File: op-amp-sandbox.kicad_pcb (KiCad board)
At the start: 2 copper layers, 14 parts, among them J1 Conn_01x06, J2 Conn_01x04, U2 TLV2372

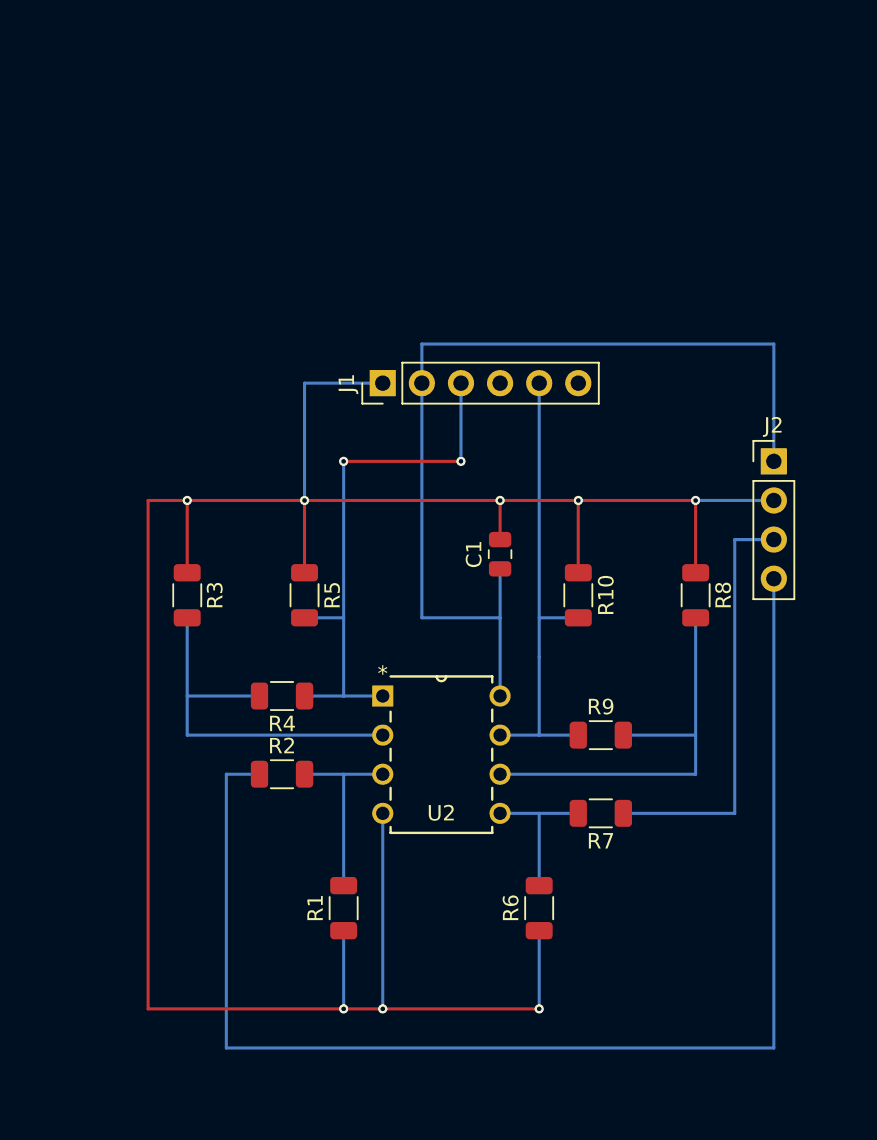
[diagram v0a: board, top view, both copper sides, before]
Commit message: Added additional pin headers to the board.
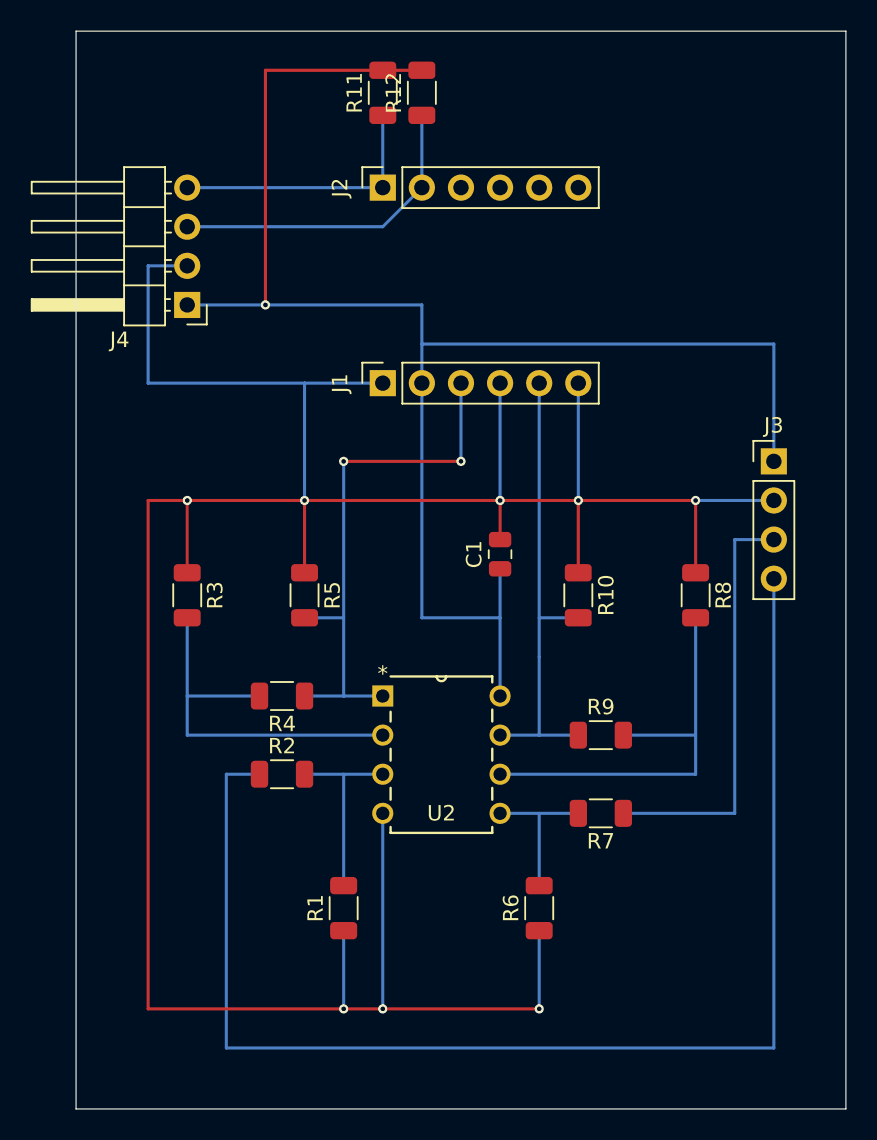
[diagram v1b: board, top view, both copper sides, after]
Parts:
- added J3: Conn_01x04, Connector_PinHeader_2.54mm:PinHeader_1x04_P2.54mm_Vertical, F.Cu at (160.0, 86.4)
- added J4: Conn_01x04, Connector_PinHeader_2.54mm:PinHeader_1x04_P2.54mm_Horizontal, F.Cu at (121.9, 76.2)
- added R11: 4.7k, Resistor_SMD:R_1206_3216Metric, F.Cu at (134.6, 62.4)
- added R12: 4.7k, Resistor_SMD:R_1206_3216Metric, F.Cu at (137.2, 62.4)
- J1: footprint Connector_PinHeader_2.54mm:PinHeader_1x06_P2.54mm_Vertical -> Connector_PinSocket_2.54mm:PinSocket_1x06_P2.54mm_Vertical
- J2: value Conn_01x04 -> Conn_01x06; footprint Connector_PinHeader_2.54mm:PinHeader_1x04_P2.54mm_Vertical -> Connector_PinSocket_2.54mm:PinSocket_1x06_P2.54mm_Vertical
- moved J2 31.0 mm to (134.6, 68.6), turned to 90 degrees
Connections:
- J1 pad 4: unconnected-(J1-Pin_4-Pad4) -> GND
- J1 pad 6: unconnected-(J1-Pin_6-Pad6) -> GND
- J2 pad 1: VCC -> SCL
- J2 pad 2: GND -> SDA
- J2 pad 3: Net-(J2-Pin_3) -> unconnected-(J2-Pin_3-Pad3)
- J2 pad 4: in -> unconnected-(J2-Pin_4-Pad4)
- R7 pad 1: Net-(J2-Pin_3) -> Net-(J3-Pin_3)
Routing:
- net VCC: track 61.6 -> 104.8 mm, vias 0 -> 1
- net GND: track 155.9 -> 191.5 mm
- net Net-(J3-Pin_3): track 0.00 -> 27.6 mm
- net Net-(J2-Pin_3): track 27.6 -> 0.00 mm
- net SDA: track 0.00 -> 21.0 mm
- net SCL: track 0.00 -> 17.4 mm
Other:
- board outline added: 50 x 70 mm
